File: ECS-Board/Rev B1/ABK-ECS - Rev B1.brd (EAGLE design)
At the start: 100 x 100 mm, 295 parts, among them J1 USB-B-S-RA, J10 22-05-7028-02, J11 RB1-125BAG1A, J12 22-05-7068-06, J13 22-05-7048-04, J14 22-05-7048-04, J15 22-05-7048-04, J2 MSTBA2, J3 22-05-7068-06, J4 22-05-7068-06, J5 22-05-7068-06, J6 22-05-7068-06, J7 22-05-7028-02, J8 FTSH-103-01-L-DV-NOPASTE, J9 FTSH-105-01-L-DV-NOPASTE, SW1 B3FS-1015, SW2 B3FS-1015, T1 MMBT2907ALT3, T10 MMBT2222AL, T11 IRLML5103TRPBF, T12 MMBT2222AL, T13 IRLML5103TRPBF, T14 IRLML5103TRPBF, T15 IRLML5103TRPBF, T16 IRLML5103TRPBF, T17 MMBT2222AL, T18 MMBT2222AL, T19 MMBT2222AL, T2 EXMACHINA-LOGO-NAME, T20 MMBT2222AL, T3 IRLML5103TRPBF, T4 IRLML5103TRPBF, T5 IRLML5103TRPBF, T6 IRLML5103TRPBF, T7 MMBT2222AL, T8 MMBT2222AL, T9 MMBT2222AL, U1 AT24C512C-SSHM-B, U2 LPC1768FBD100, U3 LT3686HDDPBF, U4 LT3686HDDPBF, U5 CD4050BD, U6 CD4050BD, U7 DP83848JSQ/NOPB, U8 SN74LVC2G17DBVR, U9 SN74LVC2G17DBVR, X1 FC-135, X2 ASE-12, X3 3000, X4 ASE_50

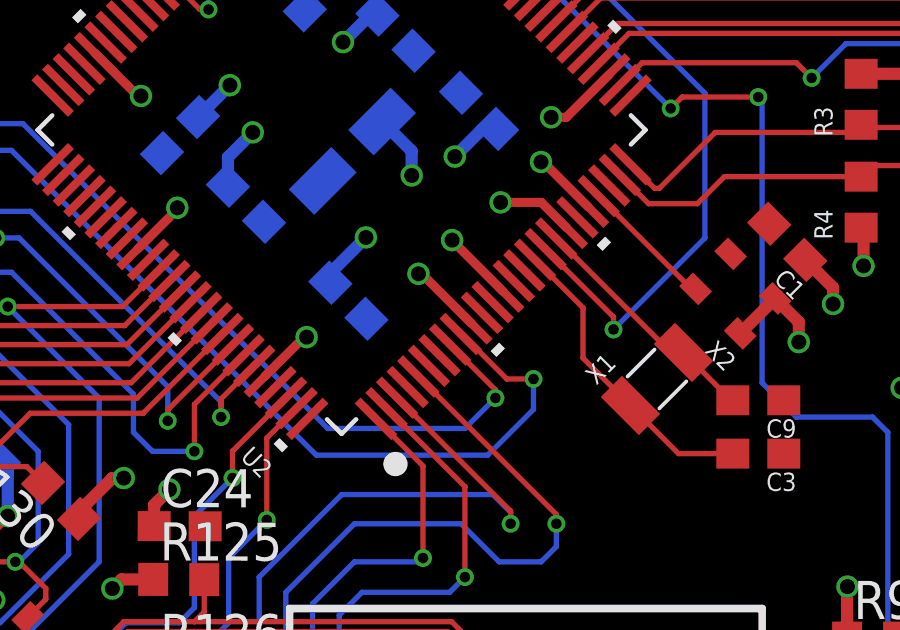
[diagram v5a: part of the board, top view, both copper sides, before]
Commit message: Add and route decoupling power for VADC
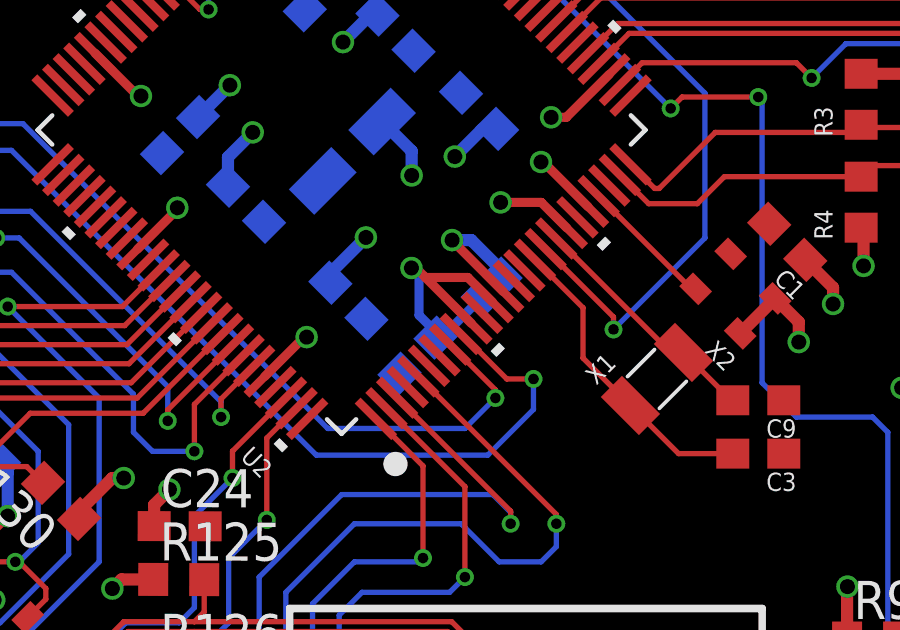
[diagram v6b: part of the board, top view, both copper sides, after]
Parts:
- added C36: 0.1uF, rcl:C0603
- added L3: 0603PS-103KLB, coilcraft:0603
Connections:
- removed net VREFP: U2.12
- new net AVDD: C36.1, J13.1, L3.P$2, U2.10, U2.12
- net +3V3: now also L3.P$1; no longer U2.10
- net GND: now also C36.2
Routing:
- net AVDD: track 0.00 -> 52.7 mm, vias 0 -> 1
- net +3V3: track 129.6 -> 129.4 mm, vias 57 -> 56
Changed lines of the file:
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@@
 <grid distance="10" unitdist="mil" unit="mm" style="lines" multiple="10" display="yes" altdistance="0.1" altunitdist="mm" altunit="mm"/>
 <layers>
-<layer number="1" name="Top" color="16" fill="1" visible="yes" active="yes"/>
-<layer number="2" name="Route2" color="17" fill="1" visible="yes" active="yes"/>
+<layer number="1" name="Top" color="16" fill="1" visible="no" active="yes"/>
+<layer number="2" name="Route2" color="17" fill="1" visible="no" active="yes"/>
 <layer number="3" name="Route3" color="4" fill="3" visible="no" active="no"/>
 <layer number="14" name="Route14" color="1" fill="6" visible="no" active="no"/>
@@
 <layer number="19" name="Unrouted" color="6" fill="1" visible="yes" active="yes"/>
 <layer number="20" name="Dimension" color="7" fill="1" visible="yes" active="yes"/>
-<layer number="21" name="tPlace" color="55" fill="1" visible="yes" active="yes"/>
+<layer number="21" name="tPlace" color="55" fill="1" visible="no" active="yes"/>
 <layer number="22" name="bPlace" color="54" fill="1" visible="yes" active="yes"/>
-<layer number="23" name="tOrigins" color="15" fill="1" visible="yes" active="yes"/>
+<layer number="23" name="tOrigins" color="15" fill="1" visible="no" active="yes"/>
 <layer number="24" name="bOrigins" color="15" fill="1" visible="yes" active="yes"/>
 <layer number="25" name="tNames" color="55" fill="1" visible="no" active="yes"/>
-<layer number="26" name="bNames" color="54" fill="1" visible="no" active="yes"/>
+<layer number="26" name="bNames" color="54" fill="1" visible="yes" active="yes"/>
 <layer number="27" name="tValues" color="53" fill="1" visible="no" active="yes"/>
-<layer number="28" name="bValues" color="52" fill="1" visible="no" active="yes"/>
+<layer number="28" name="bValues" color="52" fill="1" visible="yes" active="yes"/>
 <layer number="29" name="tStop" color="7" fill="3" visible="no" active="yes"/>
 <layer number="30" name="bStop" color="7" fill="6" visible="no" active="yes"/>
@@
 <layer number="46" name="Milling" color="35" fill="1" visible="no" active="yes"/>
 <layer number="47" name="Measures" color="21" fill="1" visible="yes" active="yes"/>
-<layer number="48" name="Document" color="24" fill="1" visible="no" active="yes"/>
+<layer number="48" name="Document" color="24" fill="1" visible="yes" active="yes"/>
 <layer number="49" name="Reference" color="48" fill="1" visible="no" active="yes"/>
 <layer number="50" name="dxf" color="7" fill="1" visible="no" active="yes"/>
 <layer number="51" name="tDocu" color="55" fill="1" visible="no" active="yes"/>
-<layer number="52" name="bDocu" color="54" fill="1" visible="no" active="yes"/>
+<layer number="52" name="bDocu" color="54" fill="1" visible="yes" active="yes"/>
 <layer number="53" name="tGND_GNDA" color="7" fill="1" visible="no" active="yes"/>
 <layer number="54" name="bGND_GNDA" color="7" fill="1" visible="no" active="yes"/>
@@
 </variantdefs>
 <classes>
-<class number="0" name="Default" width="0.1778" drill="0">
+<class number="0" name="Default" width="0" drill="0">
 </class>
 <class number="1" name="signal" width="0.1778" drill="0.35">
 </class>
-<class number="2" name="supply" width="0.4064" drill="0.5">
+<class number="2" name="supply" width="0.007740625" drill="0.5">
 </class>
 </classes>
@@
 <attribute name="OC_NEWARK" value="68R0045" x="65.532" y="19.558" size="1.778" layer="27" rot="R270" display="off"/>
 </element>
+<element name="L3" library="coilcraft" package="0603" value="0603PS-103KLB" x="42.672" y="28.448" rot="MR315">
+<attribute name="MF" value="" x="42.672003125" y="36.350625" size="1.778" layer="28" rot="MR315" display="off"/>
+<attribute name="MPN" value="" x="42.672003125" y="36.350625" size="1.778" layer="28" rot="MR315" display="off"/>
+<attribute name="OC_NEWARK" value="unknown" x="42.672003125" y="36.350625" size="1.778" layer="28" rot="MR315" display="off"/>
+</element>
+<element name="C36" library="rcl" package="C0603" value="0.1uF" x="40.204" y="26.176" rot="MR315">
+<attribute name="MF" value="" x="40.204003125" y="34.078625" size="1.778" layer="28" rot="MR315" display="off"/>
+<attribute name="MPN" value="MC0603B104K160CT" x="40.204003125" y="34.078625" size="1.778" layer="28" rot="MR315" display="off"/>
+<attribute name="OC_NEWARK" value="06R4923" x="40.204003125" y="34.078625" size="1.778" layer="28" rot="MR315" display="off"/>
+</element>
 </elements>
 <signals>
@@
 <via x="2" y="30" extent="1-16" drill="0.6"/>
 <via x="60" y="98" extent="1-16" drill="0.6"/>
+<contactref element="C36" pad="2"/>
 </signal>
 <signal name="+3V3" class="2">
@@
 <wire x1="37.29775" y1="28.608784375" x2="37.29775" y2="28.933346875" width="0.4064" layer="16"/>
 <wire x1="37.29775" y1="28.933346875" x2="38.48250625" y2="30.118103125" width="0.4064" layer="16"/>
-<contactref element="U2" pad="10"/>
-<via x="40.23365625" y="28.90576875" extent="1-16" drill="0.5"/>
 <contactref element="C21" pad="1"/>
 <contactref element="U5" pad="1"/>
@@
 <wire x1="42.371590625" y1="33.73778125" x2="42.855259375" y2="33.73778125" width="0.4064" layer="16"/>
 <wire x1="36.4234125" y1="26.795409375" x2="35.111728125" y2="25.483725" width="0.3048" layer="1"/>
-<wire x1="41.998946875" y1="27.251490625" x2="40.34466875" y2="28.90576875" width="0.3048" layer="1"/>
-<wire x1="40.34466875" y1="28.90576875" x2="40.23365625" y2="28.90576875" width="0.3048" layer="1"/>
 <wire x1="43.059609375" y1="28.31215" x2="41.3561875" y2="30.015571875" width="0.3048" layer="1"/>
 <wire x1="41.3561875" y1="30.015571875" x2="41.3561875" y2="30.028303125" width="0.3048" layer="1"/>
@@
 <wire x1="67.31" y1="20.32" x2="65.62" y2="20.32" width="0.4064" layer="1"/>
 <wire x1="65.62" y1="20.32" x2="65.532" y2="20.408" width="0.4064" layer="1"/>
+<contactref element="L3" pad="P$1"/>
+<wire x1="43.12455" y1="28.900546875" x2="41.99679375" y2="30.028303125" width="0.4064" layer="16"/>
+<wire x1="41.99679375" y1="30.028303125" x2="41.3561875" y2="30.028303125" width="0.4064" layer="16"/>
 </signal>
 <signal name="JTAG_TDO" class="1">
@@
 <wire x1="27.1145" y1="45.671471875" x2="32.99040625" y2="39.795565625" width="0.1778" layer="1"/>
 </signal>
-<signal name="VREFP">
-<contactref element="U2" pad="12"/>
-</signal>
 <signal name="1">
 <contactref element="MP1" pad="1"/>
@@
 <wire x1="63.727" y1="18.708" x2="63.627" y2="18.808" width="0.15" layer="1"/>
 </signal>
+<signal name="AVDD">
+<contactref element="L3" pad="P$2"/>
+<contactref element="C36" pad="1"/>
+<contactref element="U2" pad="12"/>
+<contactref element="U2" pad="10"/>
+<wire x1="40.80504375" y1="26.777040625" x2="41.00104375" y2="26.777040625" width="0.4064" layer="16"/>
+<wire x1="41.998946875" y1="27.251490625" x2="40.46721875" y2="28.78321875" width="0.3048" layer="1"/>
+<wire x1="40.46721875" y1="28.78321875" x2="40.1504375" y2="29.1" width="0.3048" layer="1"/>
+<wire x1="40.1504375" y1="29.1" x2="40" y2="29.1" width="0.3048" layer="1"/>
+<via x="40" y="29.1" extent="1-16" drill="0.5"/>
+<wire x1="42.70605625" y1="27.958596875" x2="41.881434375" y2="28.78321875" width="0.3048" layer="1"/>
+<wire x1="41.881434375" y1="28.78321875" x2="40.46721875" y2="28.78321875" width="0.3048" layer="1"/>
+<wire x1="41.00104375" y1="26.777040625" x2="40.254" y2="27.524084375" width="0.3048" layer="16"/>
+<wire x1="42.219453125" y1="27.99545" x2="41.00104375" y2="26.777040625" width="0.3048" layer="16"/>
+<wire x1="40.254" y1="27.524084375" x2="40.254" y2="28.846" width="0.3048" layer="16"/>
+<wire x1="40.254" y1="28.846" x2="40" y2="29.1" width="0.3048" layer="16"/>
+<contactref element="J13" pad="1"/>
+<wire x1="40" y1="29.1" x2="38.84" y2="27.94" width="0.4064" layer="15"/>
+<wire x1="38.84" y1="27.94" x2="38.1" y2="27.94" width="0.4064" layer="15"/>
+<wire x1="38.1" y1="27.94" x2="33.274" y2="32.766" width="0.4064" layer="15"/>
+<wire x1="33.274" y1="32.766" x2="30.226" y2="32.766" width="0.4064" layer="15"/>
+<wire x1="30.226" y1="32.766" x2="26.924" y2="36.068" width="0.4064" layer="15"/>
+<wire x1="26.924" y1="36.068" x2="19.558" y2="36.068" width="0.4064" layer="15"/>
+<wire x1="19.558" y1="36.068" x2="10.16" y2="26.67" width="0.4064" layer="15"/>
+<wire x1="10.16" y1="26.67" x2="5.08" y2="26.67" width="0.4064" layer="15"/>
+</signal>
 </signals>

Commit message: Generated MDP files
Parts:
- removed R152: 1K, rcl:R0603
- removed SJ6, SJ7: SJNC, SparkFun-Passives:SJ_2S
- added R6: 39K, rcl:R0603
- added SJ1, SJ2: SJNC, SparkFun-Passives:SJ_2S
- C1: value 0.1uF -> 10uF; device rcl:C0603 -> rcl:CT3216
- C10, C5: value 0.1uF -> 18pF
- C12: value 2.2uF -> 0.1uF
- C14: value 1000pF -> 2.2uF
- C16: value 2.2uF -> 1000pF
- C18: value 22uF -> 2.2uF; device rcl:C0805 -> rcl:C0603
- C20: value 0.1uF -> 22uF; device rcl:C0603 -> rcl:C0805
- C22: value 4.7uF -> 0.1uF; device rcl:CT3216 -> rcl:C0603
- C23: value 100nF -> 4.7uF; device rcl:C0603 -> rcl:CT3216
- C25, C29: value 10uF -> 100nF; device rcl:CT3216 -> rcl:C0603
- C26, C30: value 100nF -> 10uF; device rcl:C0603 -> rcl:CT3216
- C3, C9: value 18pF -> 0.1uF
- C34: value 0.1uF -> 100nF
- C4: value 10uF -> 0.1uF; device rcl:CT3216 -> rcl:C0603
- L1: value 15uH -> 0603PS-103KLB; device Wurth-POWER_MAGNETICS-rev16f:WE-PD2_5848/5820 -> coilcraft:0603
- L2: value 10uH -> 15uH
- L3: value 0603PS-103KLB -> 10uH; device coilcraft:0603 -> Wurth-POWER_MAGNETICS-rev16f:WE-PD2_5848/5820
- R100, R69: value 10K -> 1K
- R104, R73: value 1K -> 1K5
- R108, R77: value 1K5 -> 4K7
- R11: value 33 -> 1K5
- R112, R81: value 4K7 -> 100
- R116, R85: value 100 -> 330
- R12: value 1K5 -> 10K
- R120: value 330 -> 0R
- R122: value 0R -> 220
- R124: value 220 -> 49.9
- R128: value 49.9 -> 4K7
- R129: value 4K7 -> 2K2
- R13: value 10K -> 0R
- R130: value 2K2 -> 1K
- R133, R138, R143, R36, R48: value 1K -> 4K7
- R135, R139, R144, R40: value 4K7 -> 1K
- R15: value 0R -> 10K
- R16, R26: value 10K -> 1K5
- R18: value 1K5 -> 31K6
- R20: value 31K6 -> 4K7
- R22: value 4K7 -> 52K3
- R23: value 52K3 -> 10K
- R24: value 10K -> 31K6
- R25: value 31K6 -> 10K
- R28: value 1K5 -> 1K
- R52: value 4K7 -> 1K5
- R61: value 1K5 -> 1K; device rcl:R0603 -> rcl:R1206
- R65, R90, R96: value 1K -> 10K; device rcl:R1206 -> rcl:R0603
- R7: value 39K -> 24K
- R8: value 24K -> 0R, DNI
- R89: value 330 -> 1K; device rcl:R0603 -> rcl:R1206
- R9: value 0R, DNI -> 33
- R91: value 10K -> 100
- R92: value 100 -> 1K; device rcl:R0603 -> rcl:R1206
- moved SJ4 121.5 mm to (4.00, 89.4), turned to 90 degrees
- moved SJ5 121.0 mm to (96.0, 90.1), turned to 90 degrees
- moved R28 95.2 mm to (35.2, 90.5), turned to 270 degrees
- moved C20 83.7 mm to (77.8, 11.4), flipped to the top, turned to 0 degrees
- moved R135 78.0 mm to (12.4, 31.8)
- moved R133 77.7 mm to (87.6, 48.5)
- moved R138 76.2 mm to (87.6, 55.6)
- moved R139 74.1 mm to (15.0, 41.0), turned to 90 degrees
- moved R144 74.0 mm to (15.0, 45.3), turned to 270 degrees
- moved R148 71.2 mm to (87.6, 50.3), turned to 180 degrees
- moved R143 70.9 mm to (87.6, 59.2), turned to 0 degrees
- moved C34 63.3 mm to (26.9, 13.6), flipped to the bottom, turned to 270 degrees
- moved C22 61.1 mm to (37.2, 70.8), turned to 270 degrees
- moved R61 53.1 mm to (51.8, 89.5), flipped to the bottom, turned to 90 degrees
- moved R122 52.4 mm to (45.1, 5.21), flipped to the bottom, turned to 90 degrees
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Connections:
- net !ISP_BOOT: now also R120.2; no longer R121.2
- net !ISP_RST: now also R121.2; no longer R122.2
- net !RESET: now also R121.1, R15.1; no longer R122.1, R16.1
- net +24V: now also C14.1, R20.2, R65.2, R90.2, R96.2; no longer C12.1, R100.2, R22.2, R69.2, R91.2
- net +3V3: now also C1.+, C22.1, C23.+, C25.1, C3.1, C30.+, C36.1, C4.1, C9.1, L1.P$1, L3.2, R12.2, R122.2, R124.1, R129.1, R139.1, R141.1, R144.1, R146.1, R15.2, R24.2, R27.2, R8.1; no longer C1.1, C10.1, C19.1, C22.+, C23.1, C29.+, C30.1, C4.+, C5.1, L2.2, L3.P$1, R124.2, R128.1, R13.2, R130.1, R140.1, R142.1, R145.1, R147.1, R16.2, R25.2, R28.2, R9.1
- net +5V: now also C19.1, L2.2, R133.1, R138.1, R143.1, R22.2, R26.2; no longer C18.1, L1.2, R135.1, R139.1, R144.1, R23.2, R27.2
- net 1: now also SJ2.2; no longer SJ4.2
- net 2: now also SJ3.2; no longer SJ5.2
- net 3: now also SJ4.2; no longer SJ6.2
- net 4: now also SJ5.2; no longer SJ7.2
- net ADC1: now also R135.2; no longer R136.2
- net ADC2: now also R132.2; no longer R133.2
- net AVDD: now also C12.1, L1.P$2; no longer C36.1, L3.P$2
- net BOOT_SELECT_P2_10: now also R120.1, R13.1; no longer R121.1, R14.1
- net BOOT_SELECT_P2_12: now also R14.1; no longer R15.1
- net ETH_RX_N: now also R127.2; no longer R128.2
- net ETH_RX_P: now also R126.2; no longer R127.2
- net ETH_TX_N: now also R125.2; no longer R126.2
- net ETH_TX_P: now also R124.2; no longer R125.2
- net GND: now also C1.-, C16.2, C22.2, C23.-, C25.2, C26.-, C29.2, C30.-, C4.2, R104.2, R128.2, R140.1, R142.1, R145.1, R147.1, R16.2, R18.1, R23.1, R25.1, R36.2, R48.2, R6.1, R61.1, R73.2, R89.1, R92.1, SJ1.1, SJ2.1; no longer C1.2, C18.2, C22.-, C23.2, C25.-, C26.2, C29.-, C30.2, C4.-, R112.2, R129.2, R141.1, R143.1, R146.1, R148.1, R18.2, R20.1, R24.1, R26.1, R40.2, R61.2, R65.1, R7.1, R81.2, R90.1, R96.1, SJ6.1, SJ7.1
- net I2C_SCL: now also R130.2, R139.2; no longer R131.2, R141.2
- net I2C_SDA: now also R136.2, R144.2; no longer R137.2, R146.2
- net INPUT1.1: now also R47.2, R51.1; no longer R48.2, R52.1
- net INPUT1.2: now also R46.2, R50.1; no longer R47.2, R51.1
- net INPUT1.3: now also R45.2, R49.1; no longer R46.2, R50.1
- net INPUT1.4: now also R44.2, R48.1; no longer R45.2, R49.1
- net INPUT2.1: now also R35.2, R39.1; no longer R36.2, R40.1
- net INPUT2.2: now also R34.2, R38.1; no longer R35.2, R39.1
- net INPUT2.3: now also R33.2, R37.1; no longer R34.2, R38.1
- net INPUT2.4: now also R32.2, R36.1; no longer R33.2, R37.1
- net MII_MODE: now also R129.2; no longer R130.2
- net MOTOR_VFQ: now also R89.2; no longer R90.2
- net N$1: now also R10.1, R11.2; no longer R11.1, R12.2
- net N$10: now also C17.1; no longer C16.1
- net N$100: now also R44.1; no longer R45.1
- net N$101: now also R41.2; no longer R42.2
- net N$102: now also R41.1; no longer R42.1
- net N$103: now also R45.1; no longer R46.1
- net N$104: now also R42.2; no longer R43.2
- net N$105: now also R42.1; no longer R43.1
- net N$106: now also R46.1; no longer R47.1
- net N$107: now also R57.1; no longer R58.1
- net N$108: now also R58.1; no longer R59.1
- net N$109: now also R59.1; no longer R60.1
- net N$11: now also C17.2, L2.1; no longer C16.2, L1.1
- net N$110: now also R47.1; no longer R48.1
- net N$111: now also R43.2; no longer R44.2
- net N$112: now also R43.1; no longer R44.1
- net N$113: now also R122.1; no longer R123.1
- net N$114: now also R7.2; no longer R8.2
- net N$115: now also R123.1; no longer R124.1
- net N$116: now also R128.1; no longer R129.1
- net N$117: now also R133.2, R150.1; no longer R134.2, R151.1
- net N$118: now also R134.2, R148.1; no longer R135.2, R149.1
- net N$119: now also R138.2, R151.1; no longer R139.2, R152.1
- net N$120: now also R149.2; no longer R150.2
- net N$121: now also R148.2; no longer R149.2
- net N$122: now also R150.2; no longer R151.2
- net N$123: now also R151.2; no longer R152.2
- net N$124: now also R143.2, R149.1; no longer R144.2, R150.1
- net N$125: now also R132.1; no longer R133.1
- net N$126: now also R135.1; no longer R136.1
- net N$127: now also R130.1; no longer R131.1
- net N$128: now also R136.1; no longer R137.1
- net N$129: now also R131.1; no longer R132.1
- net N$13: now also R24.1, R25.2; no longer R25.1, R26.2
- net N$130: now also R137.1; no longer R138.1
- net N$14: now also C18.1; no longer C17.1
- net N$15: now also C18.2, L3.1; no longer C17.2, L2.1
- net N$17: now also R100.2; no longer R101.2
- net N$18: now also R96.1; no longer R97.1
- net N$19: now also R101.2; no longer R102.2
- net N$2: now also R9.1; no longer R10.1
- net N$20: now also R97.1; no longer R98.1
- net N$21: now also R102.2; no longer R103.2
- net N$22: now also R98.1; no longer R99.1
- net N$23: now also R103.2; no longer R104.2
- net N$24: now also R99.1; no longer R100.1
- net N$25: now also R91.1; no longer R92.1
- net N$26: now also R90.1; no longer R91.1
- net N$29: now also R16.1; no longer R17.1
- net N$3: now also R17.1; no longer R18.1
- net N$30: now also R11.1, R8.2; no longer R12.1, R9.2
- net N$31: now also R69.1, R77.1, R81.1; no longer R70.1, R78.1, R82.1
- net N$33: now also R81.2; no longer R82.2
- net N$34: now also R70.1, R78.1, R82.1; no longer R71.1, R79.1, R83.1
- net N$35: now also R82.2; no longer R83.2
- net N$36: now also R71.1, R79.1, R83.1; no longer R72.1, R80.1, R84.1
- net N$37: now also R72.1, R80.1, R84.1; no longer R73.1, R81.1, R85.1
- net N$38: now also R83.2; no longer R84.2
- net N$39: now also R84.2; no longer R85.2
- net N$4: now also R18.2; no longer R19.2
- net N$40: now also R85.1; no longer R86.1
- net N$41: now also R28.2; no longer R29.2
- net N$42: now also R86.1; no longer R87.1
- net N$43: now also R88.1; no longer R89.1
- net N$44: now also R21.1; no longer R22.1
- net N$45: now also R20.1; no longer R21.1
- net N$46: now also R87.1; no longer R88.1
- net N$47: now also R29.2; no longer R30.2
- net N$48: now also R30.2; no longer R31.2
- net N$49: now also R31.2; no longer R32.2
- net N$5: now also R12.1, R13.2; no longer R13.1, R15.2
- net N$50: now also R27.1; no longer R28.1
- net N$51: now also R26.1; no longer R27.1
- net N$52: now also R31.1; no longer R32.1
- net N$53: now also R30.1; no longer R31.1
- net N$54: now also R29.1; no longer R30.1
- net N$55: now also R28.1; no longer R29.1
- net N$56: now also R52.1; no longer R53.1
- net N$57: now also R53.1; no longer R54.1
- net N$58: now also R54.1; no longer R55.1
- net N$59: now also R55.1; no longer R56.1
- net N$6: now also C15.1; no longer C14.1
- net N$61: now also R35.1; no longer R36.1
- net N$62: now also R34.1; no longer R35.1
- net N$63: now also R33.1; no longer R34.1
- net N$64: now also R32.1; no longer R33.1
- net N$65: now also R56.1; no longer R57.1
- net N$66: now also R73.1; no longer R74.1
- net N$67: now also R74.1; no longer R75.1
- net N$68: now also R75.1; no longer R76.1
- net N$69: now also R76.1; no longer R77.1
- net N$7: now also R19.2; no longer R20.2
- net N$70: now also SJ1.2; no longer SJ3.2
- net N$71: now also R65.1; no longer R66.1
- net N$72: now also R66.1; no longer R67.1
- net N$75: now also R100.1, R108.1, R112.1; no longer R101.1, R109.1, R113.1
- net N$76: now also R112.2; no longer R113.2
- net N$77: now also R67.1; no longer R68.1
- net N$78: now also R68.1; no longer R69.1
- net N$79: now also R101.1, R109.1, R113.1; no longer R102.1, R110.1, R114.1
- net N$8: now also C16.1; no longer C15.1
- net N$80: now also R113.2; no longer R114.2
- net N$81: now also R40.2; no longer R41.2
- net N$82: now also R40.1; no longer R41.1
- net N$83: now also R102.1, R110.1, R114.1; no longer R103.1, R111.1, R115.1
- net N$84: now also R69.2; no longer R70.2
- net N$85: now also R70.2; no longer R71.2
- net N$86: now also R103.1, R111.1, R115.1; no longer R104.1, R112.1, R116.1
- net N$87: now also R114.2; no longer R115.2
- net N$88: now also R115.2; no longer R116.2
- net N$89: now also R116.1; no longer R117.1
- net N$9: now also R22.1, R23.2; no longer R23.1, R24.2
- net N$90: now also R60.1; no longer R61.1
- net N$91: now also R117.1; no longer R118.1
- net N$92: now also R119.1; no longer R120.1
- net N$93: now also R118.1; no longer R119.1
- net N$94: now also R104.1; no longer R105.1
- net N$95: now also R105.1; no longer R106.1
- net N$96: now also R106.1; no longer R107.1
- net N$97: now also R107.1; no longer R108.1
- net N$98: now also R71.2; no longer R72.2
- net N$99: now also R72.2; no longer R73.2
- net OUTPUT1.1: now also R61.2; no longer R62.2
- net OUTPUT1.1_MCU: now also R85.2; no longer R86.2
- net OUTPUT1.2: now also R62.2; no longer R63.2
- net OUTPUT1.2_MCU: now also R86.2; no longer R87.2
- net OUTPUT1.3: now also R63.2; no longer R64.2
- net OUTPUT1.3_MCU: now also R87.2; no longer R88.2
- net OUTPUT1.4: now also R64.2; no longer R65.2
- net OUTPUT1.4_MCU: now also R88.2; no longer R89.2
- net OUTPUT2.1: now also R92.2; no longer R93.2
- net OUTPUT2.1_MCU: now also R116.2; no longer R117.2
- net OUTPUT2.2: now also R93.2; no longer R94.2
- net OUTPUT2.2_MCU: now also R117.2; no longer R118.2
- net OUTPUT2.3: now also R94.2; no longer R95.2
- net OUTPUT2.3_MCU: now also R118.2; no longer R119.2
- net OUTPUT2.4: now also R95.2; no longer R96.2
- net OUTPUT2.4_MCU: now also R119.2; no longer R120.2
- net OUTPUT3.2_MCU: now also R91.2; no longer R92.2
- net PFBOUT: now also C26.+, C29.1; no longer C25.+, C26.1
- net RTCX1: now also C5.1; no longer C3.1
- net RTCX2: now also C10.1; no longer C9.1
- net UART_RX: now also R131.2, R141.2; no longer R132.2, R143.2
- net UART_TX: now also R137.2, R146.2; no longer R138.2, R148.2
- net USB_D_N: now also R9.2; no longer R10.2
- net USB_D_P: now also R10.2; no longer R11.2
- net USB_V_BUS: now also R6.2, R7.1; no longer R7.2, R8.1
